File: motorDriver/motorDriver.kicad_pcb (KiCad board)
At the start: 2 copper layers, 20.1 x 21.3 mm, 8 parts, among them P1 Vcc, P2 Input, P3 Output, U1 TB6593FNG

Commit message: Updated layout for Rev 2
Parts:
- added D1: LED, LEDs:LED-0805, F.Cu at (159.4, 82.0)
- added D2: LED, LEDs:LED-0805, F.Cu at (162.8, 82.0)
- added D3: LED, LEDs:LED-0805, F.Cu at (150.2, 92.1)
- added IN1: LED, LEDs:LED-0805, F.Cu at (150.2, 89.5)
- added IN2: LED, LEDs:LED-0805, F.Cu at (150.2, 87.0)
- added R1: 1KΩ, Resistors_SMD:R_0805_HandSoldering, B.Cu at (159.4, 82.7)
- added R2: 1KΩ, Resistors_SMD:R_0805_HandSoldering, B.Cu at (162.8, 82.7)
- added R3: 1KΩ, Resistors_SMD:R_0805_HandSoldering, B.Cu at (150.9, 89.5)
- added R4: 1KΩ, Resistors_SMD:R_0805_HandSoldering, B.Cu at (150.9, 87.0)
- added R5: 1KΩ, Resistors_SMD:R_0805_HandSoldering, B.Cu at (150.9, 92.1)
- added R6: 0Ω, Resistors_SMD:R_0805_HandSoldering, F.Cu at (169.5, 87.6)
- added REF**: MountingHole_3mm, Mounting_Holes:MountingHole_3mm, F.Cu at (169.2, 100.3)
- added REF**: MountingHole_3mm, Mounting_Holes:MountingHole_3mm, F.Cu at (146.1, 100.3)
- added REF**: MountingHole_3mm, Mounting_Holes:MountingHole_3mm, F.Cu at (146.1, 78.1)
- added REF**: MountingHole_3mm, Mounting_Holes:MountingHole_3mm, F.Cu at (169.2, 78.1)
- added REF**111: Via, GoGoGo:Via, F.Cu at (149.1, 75.9)
- added REF**111111: Via, GoGoGo:Via, F.Cu at (167.4, 91.2)
- added REF**1111111: Via, GoGoGo:Via, F.Cu at (162.3, 96.3)
- added REF**111111101: Via, GoGoGo:Via, F.Cu at (155.2, 95.0)
- added REF**11111111: Via, GoGoGo:Via, F.Cu at (143.8, 95.0)
- added REF**1111111101: Via, GoGoGo:Via, F.Cu at (155.2, 96.3)
- added REF**1111111102: Via, GoGoGo:Via, F.Cu at (155.2, 97.5)
- added REF**1111111103: Via, GoGoGo:Via, F.Cu at (155.2, 98.8)
- added REF**1111111104: Via, GoGoGo:Via, F.Cu at (155.2, 100.1)
- added REF**1111111105: Via, GoGoGo:Via, F.Cu at (155.2, 101.3)
- added REF**1111111106: Via, GoGoGo:Via, F.Cu at (155.2, 102.6)
- added REF**111111111: Via, GoGoGo:Via, F.Cu at (143.8, 96.3)
- added REF**111111112: Via, GoGoGo:Via, F.Cu at (143.8, 97.5)
- added REF**111111113: Via, GoGoGo:Via, F.Cu at (143.8, 98.8)
- added REF**111111121: Via, GoGoGo:Via, F.Cu at (145.0, 96.3)
- added REF**111111122: Via, GoGoGo:Via, F.Cu at (145.0, 97.5)
- added REF**111111126: Via, GoGoGo:Via, F.Cu at (156.7, 96.3)
- added REF**111111131: Via, GoGoGo:Via, F.Cu at (146.3, 96.3)
- added REF**111111132: Via, GoGoGo:Via, F.Cu at (146.3, 97.5)
- added REF**111111136: Via, GoGoGo:Via, F.Cu at (156.7, 97.5)
- added REF**111111137: Via, GoGoGo:Via, F.Cu at (156.7, 95.0)
- added REF**111111138: Via, GoGoGo:Via, F.Cu at (156.7, 102.6)
- added REF**111111141: Via, GoGoGo:Via, F.Cu at (147.6, 96.3)
- added REF**111111142: Via, GoGoGo:Via, F.Cu at (147.6, 97.5)
- added REF**111111146: Via, GoGoGo:Via, F.Cu at (156.7, 98.8)
- added REF**111111147: Via, GoGoGo:Via, F.Cu at (156.7, 100.1)
- added REF**111111148: Via, GoGoGo:Via, F.Cu at (156.7, 101.3)
- added REF**111111151: Via, GoGoGo:Via, F.Cu at (148.8, 96.3)
- added REF**111111152: Via, GoGoGo:Via, F.Cu at (148.8, 97.5)
- added REF**111111153: Via, GoGoGo:Via, F.Cu at (148.8, 98.8)
- added REF**111111156: Via, GoGoGo:Via, F.Cu at (148.8, 102.6)
- added REF**111111161: Via, GoGoGo:Via, F.Cu at (150.1, 96.3)
- added REF**111111162: Via, GoGoGo:Via, F.Cu at (150.1, 97.5)
- added REF**111111163: Via, GoGoGo:Via, F.Cu at (150.1, 98.8)
- added REF**111111164: Via, GoGoGo:Via, F.Cu at (150.1, 100.1)
- added REF**111111165: Via, GoGoGo:Via, F.Cu at (150.1, 101.3)
- added REF**111111166: Via, GoGoGo:Via, F.Cu at (150.1, 102.6)
- added REF**111111171: Via, GoGoGo:Via, F.Cu at (151.4, 96.3)
- added REF**111111172: Via, GoGoGo:Via, F.Cu at (151.4, 97.5)
- added REF**111111173: Via, GoGoGo:Via, F.Cu at (151.4, 98.8)
- added REF**111111174: Via, GoGoGo:Via, F.Cu at (151.4, 100.1)
- added REF**111111175: Via, GoGoGo:Via, F.Cu at (151.4, 101.3)
- added REF**111111176: Via, GoGoGo:Via, F.Cu at (151.4, 102.6)
- added REF**111111181: Via, GoGoGo:Via, F.Cu at (152.7, 96.3)
- added REF**111111182: Via, GoGoGo:Via, F.Cu at (152.7, 97.5)
- added REF**111111183: Via, GoGoGo:Via, F.Cu at (152.7, 98.8)
- added REF**111111184: Via, GoGoGo:Via, F.Cu at (152.7, 100.1)
- added REF**111111185: Via, GoGoGo:Via, F.Cu at (152.7, 101.3)
- added REF**111111186: Via, GoGoGo:Via, F.Cu at (152.7, 102.6)
- added REF**111111191: Via, GoGoGo:Via, F.Cu at (153.9, 96.3)
- added REF**111111192: Via, GoGoGo:Via, F.Cu at (153.9, 97.5)
- added REF**111111193: Via, GoGoGo:Via, F.Cu at (153.9, 98.8)
- added REF**111111194: Via, GoGoGo:Via, F.Cu at (153.9, 100.1)
- added REF**111111195: Via, GoGoGo:Via, F.Cu at (153.9, 101.3)
- added REF**111111196: Via, GoGoGo:Via, F.Cu at (153.9, 102.6)
- added REF**1111112: Via, GoGoGo:Via, F.Cu at (162.3, 97.5)
- added REF**11111121: Via, GoGoGo:Via, F.Cu at (145.0, 95.0)
- added REF**1111113: Via, GoGoGo:Via, F.Cu at (162.3, 98.8)
- added REF**11111131: Via, GoGoGo:Via, F.Cu at (146.3, 95.0)
- added REF**11111141: Via, GoGoGo:Via, F.Cu at (147.6, 95.0)
- added REF**11111151: Via, GoGoGo:Via, F.Cu at (148.8, 95.0)
- added REF**11111161: Via, GoGoGo:Via, F.Cu at (150.1, 95.0)
- added REF**11111171: Via, GoGoGo:Via, F.Cu at (151.4, 95.0)
- added REF**11111181: Via, GoGoGo:Via, F.Cu at (152.7, 95.0)
- added REF**11111191: Via, GoGoGo:Via, F.Cu at (153.9, 95.0)
- added REF**111112: Via, GoGoGo:Via, F.Cu at (167.4, 92.5)
- added REF**1111121: Via, GoGoGo:Via, F.Cu at (163.6, 96.3)
- added REF**1111122: Via, GoGoGo:Via, F.Cu at (163.6, 97.5)
- added REF**1111123: Via, GoGoGo:Via, F.Cu at (163.6, 98.8)
- added REF**1111124: Via, GoGoGo:Via, F.Cu at (163.6, 100.1)
- added REF**1111125: Via, GoGoGo:Via, F.Cu at (163.6, 101.3)
- added REF**1111126: Via, GoGoGo:Via, F.Cu at (163.6, 102.6)
- added REF**111113: Via, GoGoGo:Via, F.Cu at (167.4, 93.7)
- added REF**1111131: Via, GoGoGo:Via, F.Cu at (164.8, 96.3)
- added REF**1111132: Via, GoGoGo:Via, F.Cu at (164.8, 97.5)
- added REF**1111133: Via, GoGoGo:Via, F.Cu at (164.8, 98.8)
- added REF**1111134: Via, GoGoGo:Via, F.Cu at (164.8, 100.1)
- added REF**1111135: Via, GoGoGo:Via, F.Cu at (164.8, 101.3)
- added REF**1111136: Via, GoGoGo:Via, F.Cu at (164.8, 102.6)
- added REF**111114: Via, GoGoGo:Via, F.Cu at (167.4, 95.0)
- added REF**1111141: Via, GoGoGo:Via, F.Cu at (166.1, 96.3)
- added REF**1111142: Via, GoGoGo:Via, F.Cu at (166.1, 97.5)
- added REF**1111143: Via, GoGoGo:Via, F.Cu at (166.1, 98.8)
- added REF**1111144: Via, GoGoGo:Via, F.Cu at (166.1, 100.1)
- added REF**1111145: Via, GoGoGo:Via, F.Cu at (166.1, 101.3)
- added REF**1111146: Via, GoGoGo:Via, F.Cu at (166.1, 102.6)
- added REF**111115: Via, GoGoGo:Via, F.Cu at (167.4, 96.3)
- added REF**111116: Via, GoGoGo:Via, F.Cu at (167.4, 97.5)
- added REF**111121: Via, GoGoGo:Via, F.Cu at (168.7, 91.2)
- added REF**111122: Via, GoGoGo:Via, F.Cu at (168.7, 92.5)
- added REF**111123: Via, GoGoGo:Via, F.Cu at (168.7, 93.7)
- added REF**111124: Via, GoGoGo:Via, F.Cu at (168.7, 95.0)
- added REF**111125: Via, GoGoGo:Via, F.Cu at (168.7, 96.3)
- added REF**111126: Via, GoGoGo:Via, F.Cu at (168.7, 97.5)
- added REF**111131: Via, GoGoGo:Via, F.Cu at (169.9, 91.2)
- added REF**111132: Via, GoGoGo:Via, F.Cu at (169.9, 92.5)
- added REF**111133: Via, GoGoGo:Via, F.Cu at (169.9, 93.7)
- added REF**111134: Via, GoGoGo:Via, F.Cu at (169.9, 95.0)
- added REF**111135: Via, GoGoGo:Via, F.Cu at (169.9, 96.3)
- added REF**111136: Via, GoGoGo:Via, F.Cu at (169.9, 97.5)
- added REF**111141: Via, GoGoGo:Via, F.Cu at (171.2, 91.2)
- added REF**111142: Via, GoGoGo:Via, F.Cu at (171.2, 92.5)
- added REF**111143: Via, GoGoGo:Via, F.Cu at (171.2, 93.7)
- added REF**111144: Via, GoGoGo:Via, F.Cu at (171.2, 95.0)
- added REF**111145: Via, GoGoGo:Via, F.Cu at (171.2, 96.3)
- added REF**111146: Via, GoGoGo:Via, F.Cu at (171.2, 97.5)
- added REF**112: Via, GoGoGo:Via, F.Cu at (149.1, 77.2)
- added REF**113: Via, GoGoGo:Via, F.Cu at (149.1, 78.5)
- added REF**114: Via, GoGoGo:Via, F.Cu at (149.1, 79.8)
- added REF**115: Via, GoGoGo:Via, F.Cu at (149.1, 81.0)
- added REF**116: Via, GoGoGo:Via, F.Cu at (149.1, 82.3)
- added REF**118: Via, GoGoGo:Via, F.Cu at (156.7, 87.1)
- added REF**118: Via, GoGoGo:Via, F.Cu at (154.7, 86.4)
- added REF**118: Via, GoGoGo:Via, F.Cu at (158.9, 90.3)
- added REF**118: Via, GoGoGo:Via, F.Cu at (151.6, 84.3)
- added REF**118: Via, GoGoGo:Via, F.Cu at (149.1, 85.6)
- added REF**118: Via, GoGoGo:Via, F.Cu at (150.4, 84.3)
- added REF**118: Via, GoGoGo:Via, F.Cu at (154.7, 88.9)
- added REF**118: Via, GoGoGo:Via, F.Cu at (149.1, 84.3)
- added REF**121: Via, GoGoGo:Via, F.Cu at (150.4, 75.9)
- added REF**122: Via, GoGoGo:Via, F.Cu at (150.4, 77.2)
- added REF**123: Via, GoGoGo:Via, F.Cu at (150.4, 78.5)
- added REF**124: Via, GoGoGo:Via, F.Cu at (150.4, 79.8)
- added REF**125: Via, GoGoGo:Via, F.Cu at (150.4, 81.0)
- added REF**126: Via, GoGoGo:Via, F.Cu at (150.4, 82.3)
- added REF**128: Via, GoGoGo:Via, F.Cu at (155.4, 83.6)
- added REF**131: Via, GoGoGo:Via, F.Cu at (151.6, 75.9)
- added REF**132: Via, GoGoGo:Via, F.Cu at (151.6, 77.2)
- added REF**133: Via, GoGoGo:Via, F.Cu at (151.6, 78.5)
- added REF**134: Via, GoGoGo:Via, F.Cu at (151.6, 79.8)
- added REF**135: Via, GoGoGo:Via, F.Cu at (151.6, 81.0)
- added REF**136: Via, GoGoGo:Via, F.Cu at (151.6, 82.3)
- added REF**138: Via, GoGoGo:Via, F.Cu at (155.4, 82.3)
- added REF**141: Via, GoGoGo:Via, F.Cu at (152.9, 75.9)
- added REF**142: Via, GoGoGo:Via, F.Cu at (152.9, 77.2)
- added REF**143: Via, GoGoGo:Via, F.Cu at (152.9, 78.5)
- added REF**144: Via, GoGoGo:Via, F.Cu at (152.9, 79.8)
- added REF**145: Via, GoGoGo:Via, F.Cu at (152.9, 81.0)
- added REF**146: Via, GoGoGo:Via, F.Cu at (152.9, 82.3)
- added REF**148: Via, GoGoGo:Via, F.Cu at (155.4, 81.0)
- added REF**151: Via, GoGoGo:Via, F.Cu at (154.2, 75.9)
- added REF**152: Via, GoGoGo:Via, F.Cu at (154.2, 77.2)
- added REF**153: Via, GoGoGo:Via, F.Cu at (154.2, 78.5)
- added REF**154: Via, GoGoGo:Via, F.Cu at (154.2, 79.8)
- added REF**155: Via, GoGoGo:Via, F.Cu at (154.2, 81.0)
- added REF**156: Via, GoGoGo:Via, F.Cu at (154.2, 82.3)
- added REF**158: Via, GoGoGo:Via, F.Cu at (155.4, 79.8)
- P1: value Vcc -> CONN_01X03; footprint Pin_Headers:Pin_Header_Straight_1x02 -> Pin_Headers:Pin_Header_Straight_1x03
- moved P2 6.07 mm to (144.8, 84.5)
- moved P1 6.03 mm to (161.9, 76.8)
- moved P3 2.54 mm to (159.0, 101.6)
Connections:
- C1 pad 1: /VM -> /Vcc
- C2 pad 1: /VM -> /Vcc
- P1 pad 2: GND -> /Vcc
- U1 pad 20: /VM -> /Vcc
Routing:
- net GND: track 117.2 -> 0.27 mm, vias 84 -> 0
- net /Vcc: track 0.00 -> 32.9 mm
- net /PMW: track 11.3 -> 19.2 mm
- net /IN1: track 13.2 -> 19.2 mm, vias 2 -> 0
- net /STBY: track 7.15 -> 12.8 mm
- net /IN2: track 14.0 -> 19.5 mm, vias 2 -> 0
- net Net-(IN2-Pad1): track 0.00 -> 5.49 mm, vias 0 -> 1
- net Net-(IN1-Pad1): track 0.00 -> 4.44 mm, vias 0 -> 1
- net Net-(D1-Pad1): track 0.00 -> 4.20 mm, vias 0 -> 1
- net Net-(D2-Pad1): track 0.00 -> 3.94 mm, vias 0 -> 1
- net Net-(D3-Pad1): track 0.00 -> 3.69 mm, vias 0 -> 1
- net /VM: track 44.6 -> 47.7 mm
- net /O2: track 10.1 -> 12.7 mm
- net /O1: track 9.90 -> 12.4 mm
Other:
- board size 20.1 x 21.3 mm -> 29.5 x 28.7 mm
- board text added: "Go! Go! Go! Motor Driver Rev 2L.3"
- board text added: "O1 O2"
- board text added: "PWM"
- board text added: "Vcc VM"
- board text removed: "IN1"
- board text removed: "IN2"
- board text removed: "Motor Driver Rev 2L.2"
- board text removed: "O1"
- board text removed: "O2"
- board text removed: "PMW"
- board text removed: "Vcc"

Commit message: Generated Gerbers for Rev2
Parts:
- removed REF**111111, REF**111112, REF**111121: Via, GoGoGo:Via
- added REF**111141: Via, GoGoGo:Via, F.Cu at (169.9, 83.6)
- added REF**111141: Via, GoGoGo:Via, F.Cu at (168.7, 82.3)
- added REF**111141: Via, GoGoGo:Via, F.Cu at (169.9, 82.3)
- added REF**111141: Via, GoGoGo:Via, F.Cu at (171.2, 82.3)
- added REF**111141: Via, GoGoGo:Via, F.Cu at (171.2, 83.6)
- added REF**111142: Via, GoGoGo:Via, F.Cu at (169.9, 84.8)
- added REF**111142: Via, GoGoGo:Via, F.Cu at (171.2, 84.8)
- added REF**111143: Via, GoGoGo:Via, F.Cu at (169.9, 86.1)
- added REF**111143: Via, GoGoGo:Via, F.Cu at (171.2, 86.1)
- added REF**111144: Via, GoGoGo:Via, F.Cu at (169.9, 87.4)
- added REF**111144: Via, GoGoGo:Via, F.Cu at (171.2, 87.4)
- added REF**111145: Via, GoGoGo:Via, F.Cu at (171.2, 88.6)
- added REF**111146: Via, GoGoGo:Via, F.Cu at (171.2, 89.9)
- moved R6 2.72 mm to (167.4, 89.3), turned to 0 degrees
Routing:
- net /VM: track 47.7 -> 43.4 mm
- net /Vcc: track 32.9 -> 29.6 mm
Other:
- board text added: "Go! Go! Go! Motor Driver Rev 2L.3-b33e3c8"
- board text removed: "Go! Go! Go! Motor Driver Rev 2L.3"

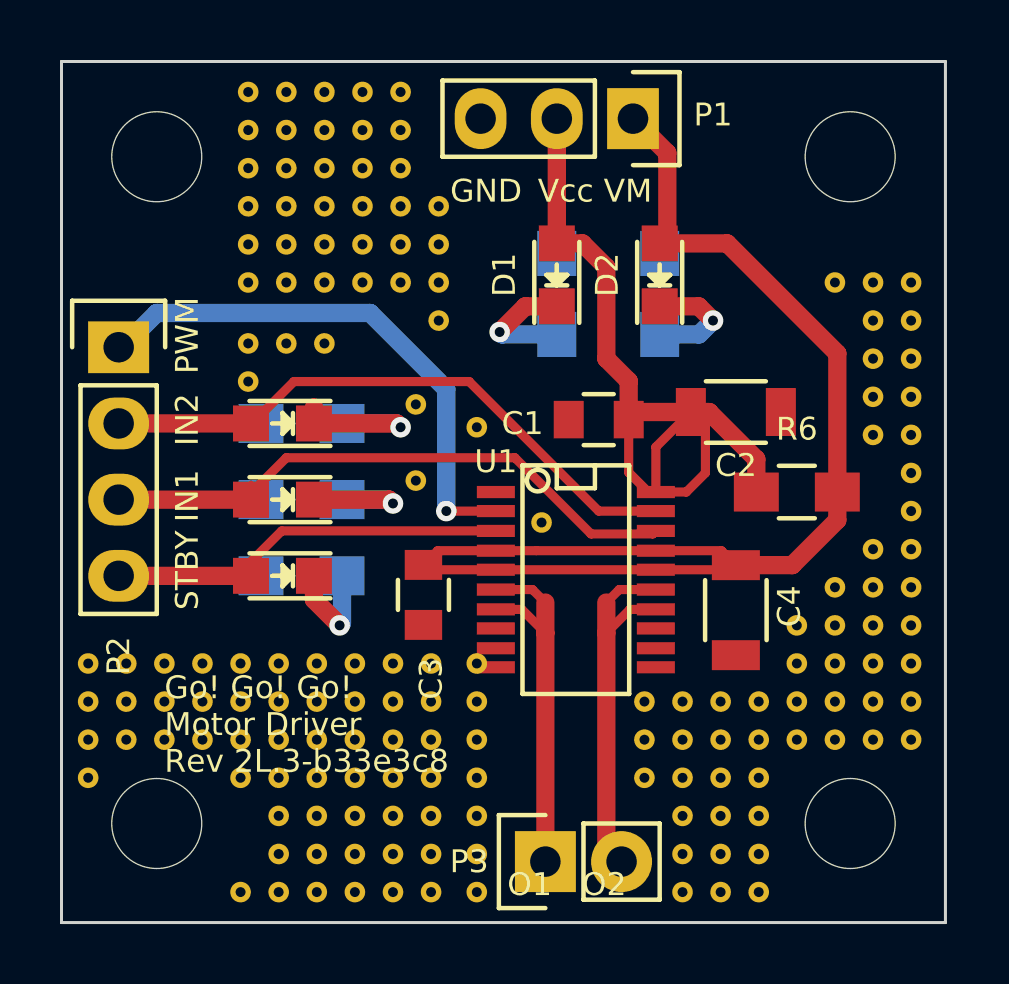
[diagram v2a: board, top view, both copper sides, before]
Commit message: Shifted the title label to the back
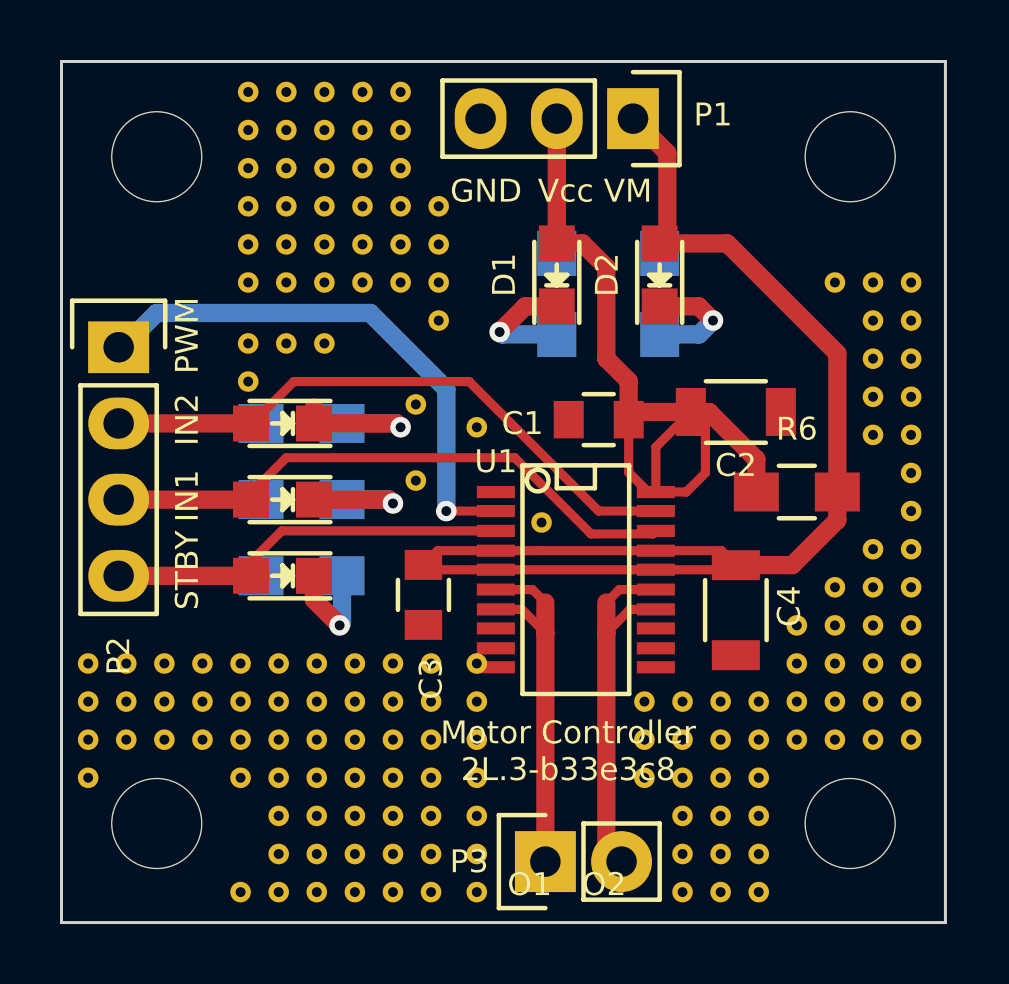
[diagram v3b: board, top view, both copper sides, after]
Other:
- board text added: "Motor Controller 2L.3-b33e3c8"
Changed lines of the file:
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@@
     (area 142.824999 74.879999 172.389001 103.682001)
     (thickness 1.6)
-    (drawings 10)
+    (drawings 11)
     (tracks 116)
     (zones 0)
@@
   )
   (setup
-    (last_trace_width 0.6096)
+    (last_trace_width 0.1524)
     (user_trace_width 0.3048)
     (user_trace_width 0.6096)
@@
       (net 1 GND) (zone_connect 2))
   )
+  (gr_text "Motor Controller\n2L.3-b33e3c8" (at 159.766 97.917) (layer F.SilkS)
+    (effects (font (size 0.762 0.762) (thickness 0.127)))
+  )
   (gr_line (start 142.875 103.632) (end 142.875 74.93) (angle 90) (layer Edge.Cuts) (width 0.1))
   (gr_line (start 172.339 103.632) (end 142.875 103.632) (angle 90) (layer Edge.Cuts) (width 0.1))
   (gr_line (start 172.339 74.93) (end 172.339 103.632) (angle 90) (layer Edge.Cuts) (width 0.1))
   (gr_line (start 142.875 74.93) (end 172.339 74.93) (angle 90) (layer Edge.Cuts) (width 0.1))
-  (gr_text "Go! Go! Go!\nMotor Driver \nRev 2L.3-b33e3c8" (at 146.304 97.028) (layer F.SilkS)
-    (effects (font (size 0.762 0.762) (thickness 0.127)) (justify left))
+  (gr_text "Go! Go! Go!\nMotor Driver \nRev 2L.3-b33e3c8" (at 167.386 88.011) (layer B.SilkS)
+    (effects (font (size 0.762 0.762) (thickness 0.127)) (justify left mirror))
   )
   (gr_text GND (at 155.829 79.248) (layer F.SilkS)

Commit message: Corrected a stitching via on ground pins
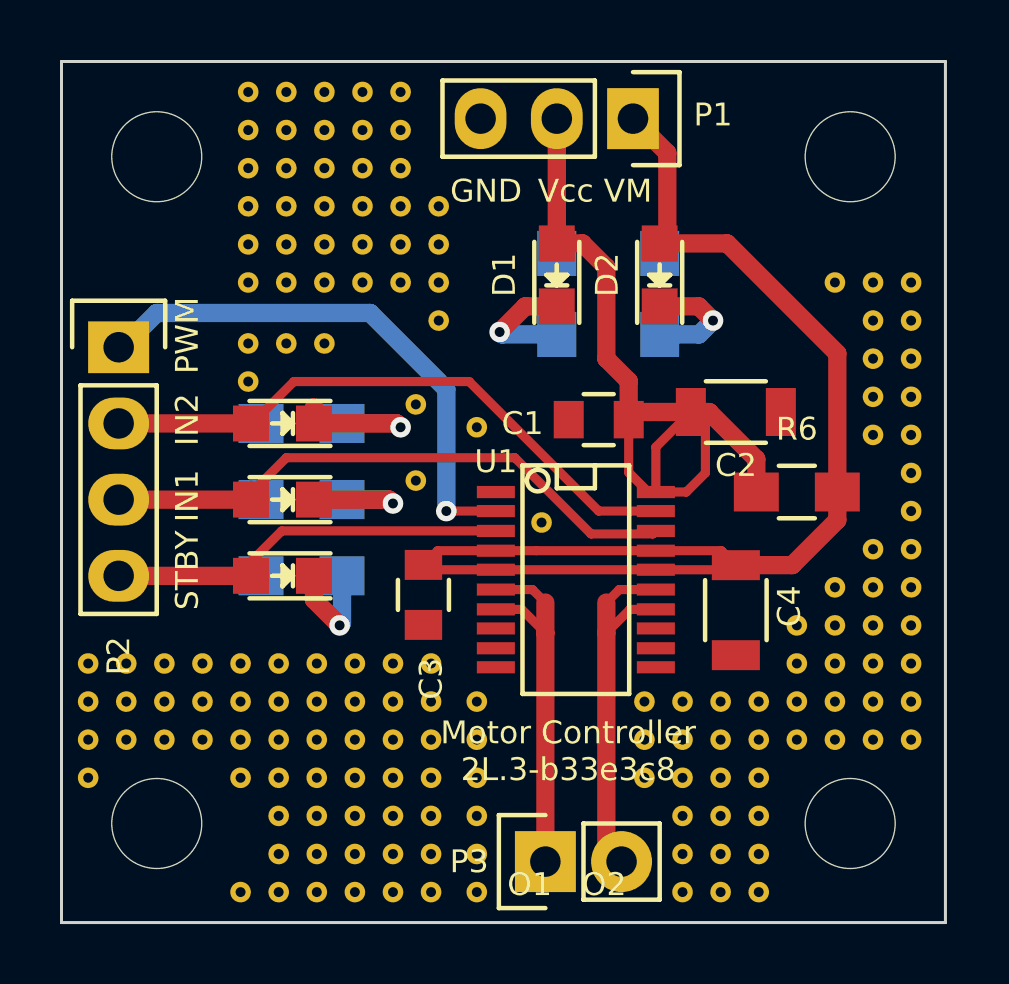
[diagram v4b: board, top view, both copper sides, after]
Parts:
- removed REF**111111137: Via, GoGoGo:Via
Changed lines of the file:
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@@
-(kicad_pcb (version 4) (host pcbnew 0.201508140901+6091~28~ubuntu14.04.1-product)
+(kicad_pcb (version 4) (host pcbnew 4.0.0-rc1-stable)
   (general
-    (links 202)
+    (links 201)
     (no_connects 0)
-    (area 142.824999 74.879999 172.389001 103.682001)
+    (area 137.108028 72.9361 176.423401 106.08056)
     (thickness 1.6)
     (drawings 11)
     (tracks 116)
     (zones 0)
-    (modules 180)
+    (modules 179)
     (nets 15)
   )
@@
       (effects (font (size 1 1) (thickness 0.15)))
     )
-    (fp_text value Via (at 0 1.27) (layer F.Fab) hide
-      (effects (font (size 1 1) (thickness 0.15)))
-    )
-    (pad 1 thru_hole circle (at 0 0) (size 0.6858 0.6858) (drill 0.3302) (layers *.Cu *.Mask F.SilkS)
-      (net 1 GND) (zone_connect 2))
-  )
-  (module GoGoGo:Via (layer F.Cu)
-    (at 156.718 94.996)
-    (fp_text reference REF**111111137 (at 0 -1.27) (layer F.SilkS) hide
-      (effects (font (size 1 1) (thickness 0.15)))
-    )
